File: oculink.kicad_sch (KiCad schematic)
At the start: 28 parts, among them J4 OCuLink_x4_Amphenol_G14A42121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, U2 MAX3373EEKA+

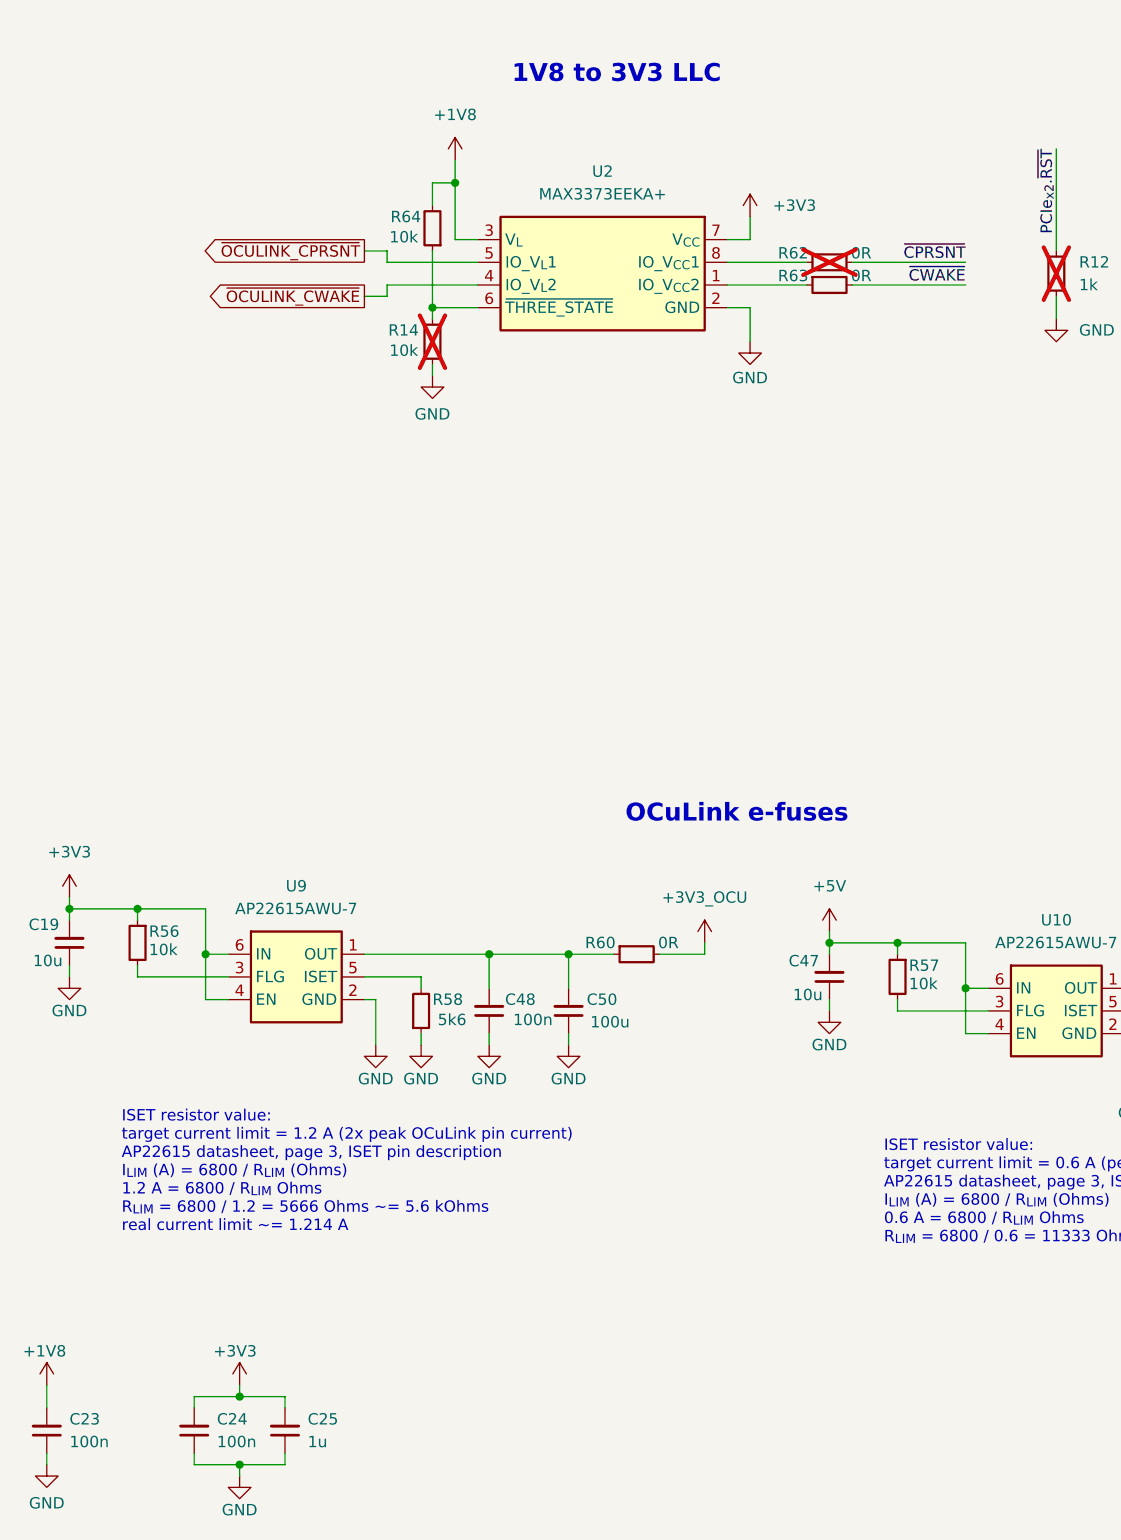
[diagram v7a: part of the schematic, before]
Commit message: [#100765] Prettify decoupling caps
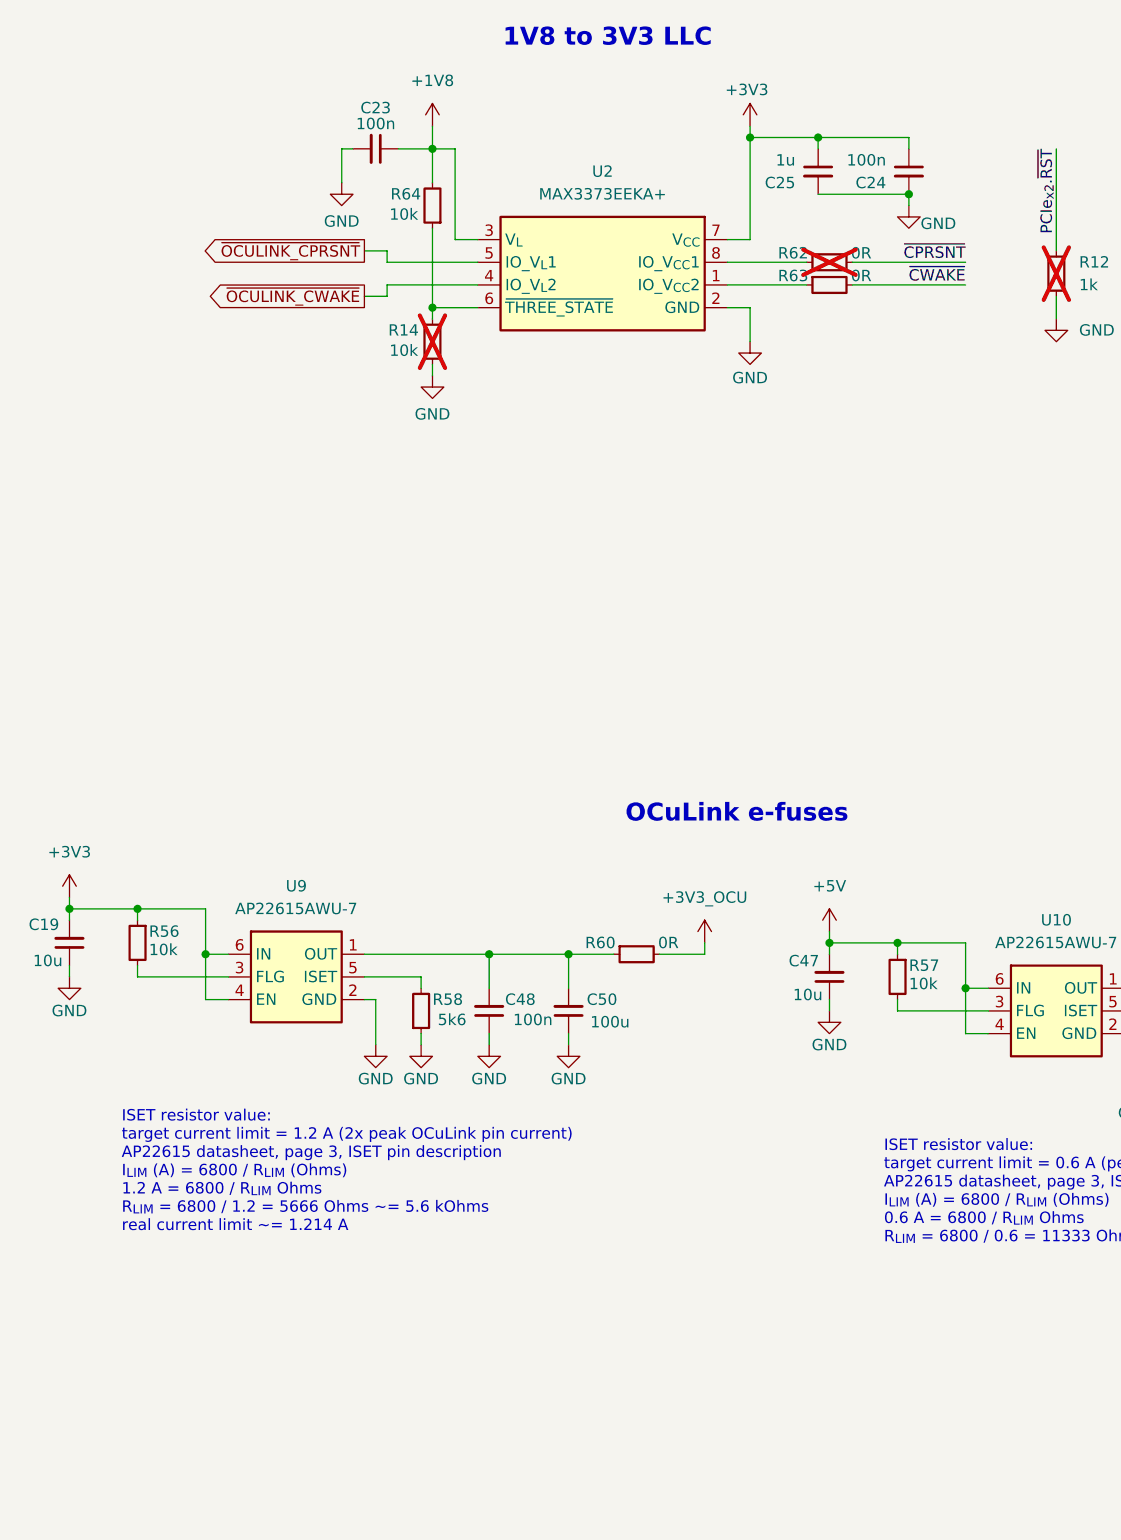
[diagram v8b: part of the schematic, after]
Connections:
- net +1V8: now also C23.1; no longer C23.2
- net +3V3: now also C24.1, C25.1; no longer C24.2, C25.2
- net GND: now also C23.2, C24.2, C25.2; no longer C23.1, C24.1, C25.1
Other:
- moved on the sheet: C23, C24, C25, R64
